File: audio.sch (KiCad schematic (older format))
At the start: 20 parts, among them P9 AUDIO LINE OUT, U5 I²S AUDIO DAC

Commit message: Cambios menores
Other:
- note added: "Decoupling capacitors. \nPlace as close as possible to the affected IC pin."
- moved on the sheet: C17, C25, C26, C27, C28, C29, C30, D3, R38, R40

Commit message: Nuevo layout, mejoras y modificaciones del revisor
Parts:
- U5: symbol PCM5100A-RESCUE-retro-ciaa -> PCM5100A
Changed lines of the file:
@@
 LIBS:contrib
 LIBS:valves
-LIBS:salmon
+LIBS:retro-ciaa
 LIBS:retro-ciaa-cache
 EELAYER 25 0
@@
 encoding utf-8
 Sheet 4 8
-Title "RETRO-CIAA / AUDIO"
-Date "2018-10-19"
+Title "AUDIO OUTPUT"
+Date "2018-10-20"
 Rev "1.1.1"
-Comp "Salmon Robotics"
+Comp "http://www.retro-ciaa.com"
 Comment1 "All resistors 1% & 0603\" unless otherwise noted"
 Comment2 "ERC check OK on 2018-10-19"
@@
 $EndDescr
 $Comp
-L PCM5100A-RESCUE-retro-ciaa U5
+L PCM5100A U5
 U 1 1 5BD13A7B
 P 7600 2100

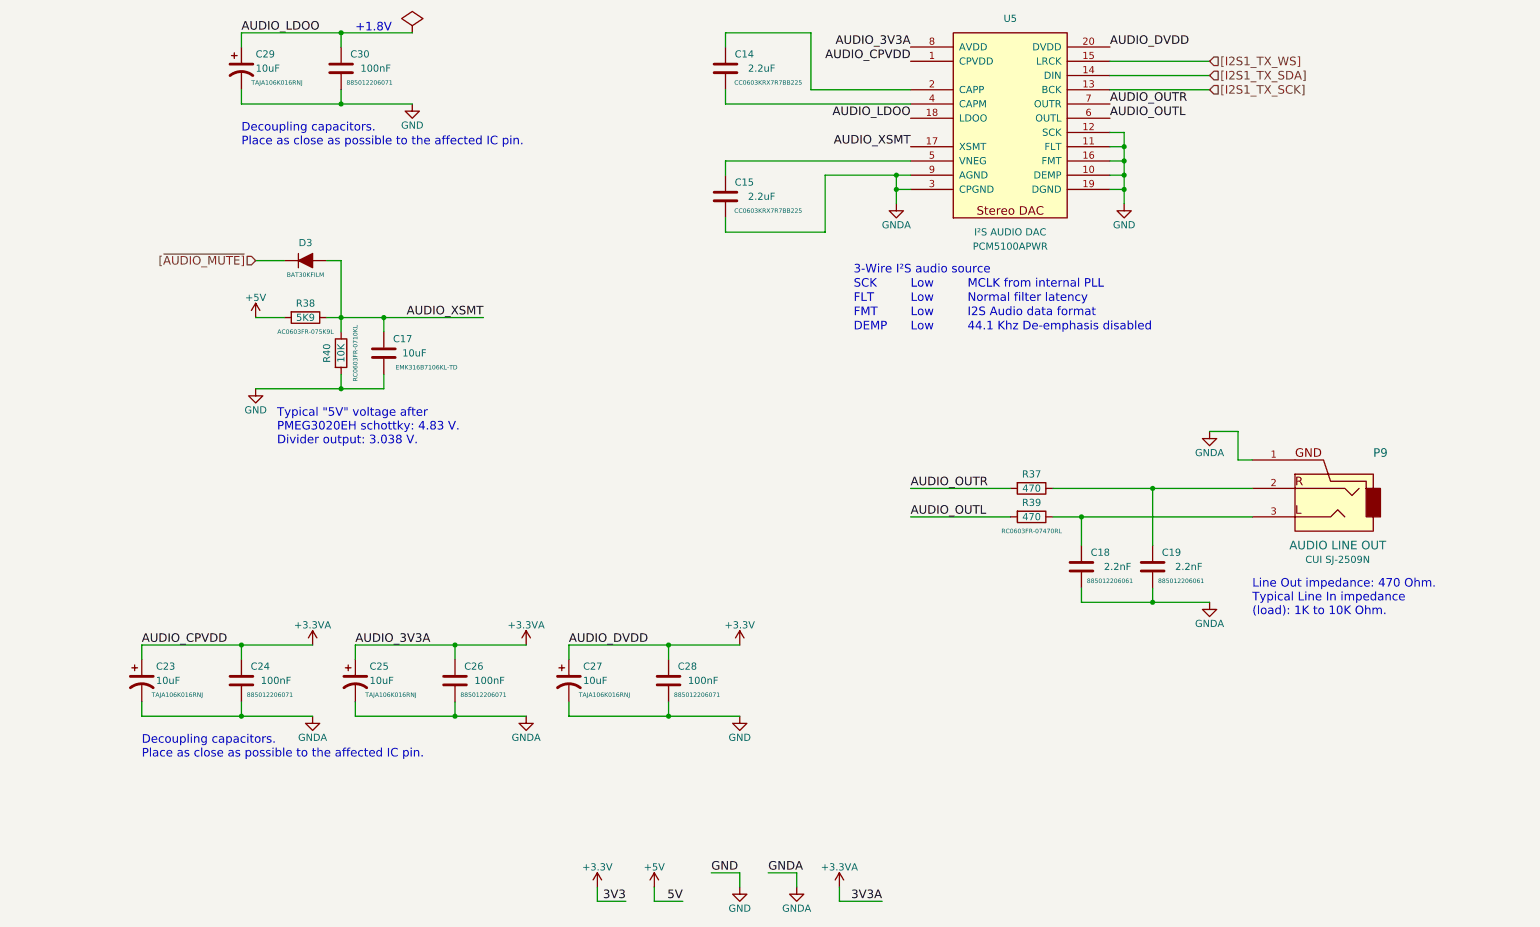
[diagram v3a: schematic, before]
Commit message: Se agrego indice en pagina 1. Union de islas de componentes con cables
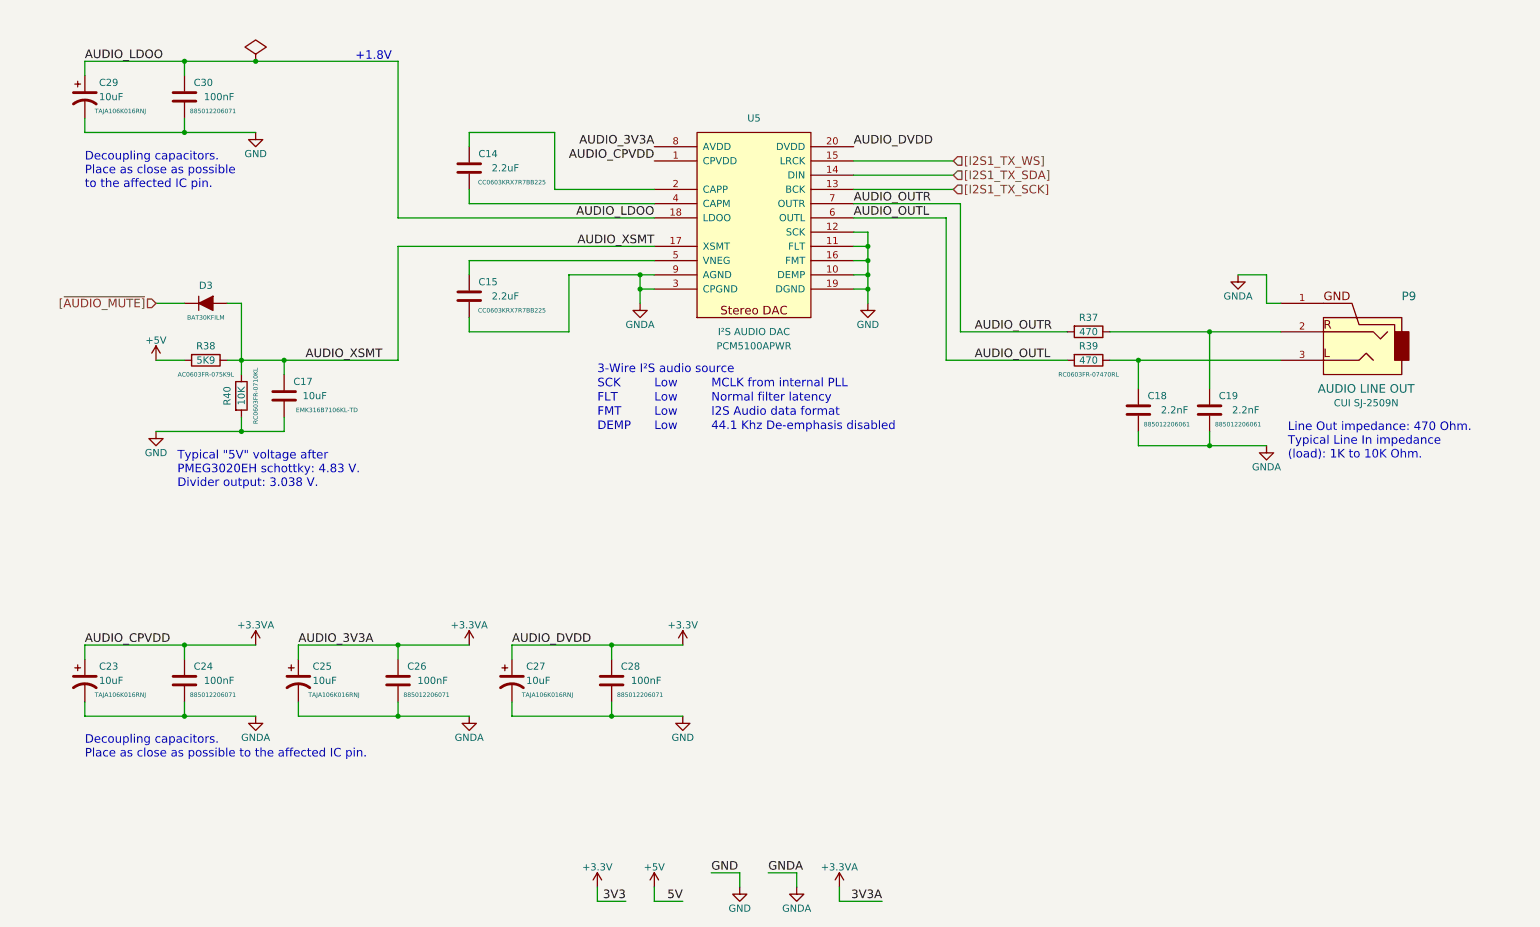
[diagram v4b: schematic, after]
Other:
- note added: "Decoupling capacitors. \nPlace as close as possible\nto the affected IC pin."
- moved on the sheet: C14, C15, C17, C18, C19, C23, C24, C25, C26, C27, C28, C29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

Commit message: Limpieza de etiquetas de alimentacion
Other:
- moved on the sheet: C23, C24, C25, C26, C27, C28
